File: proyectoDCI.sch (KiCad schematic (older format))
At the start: 0 parts

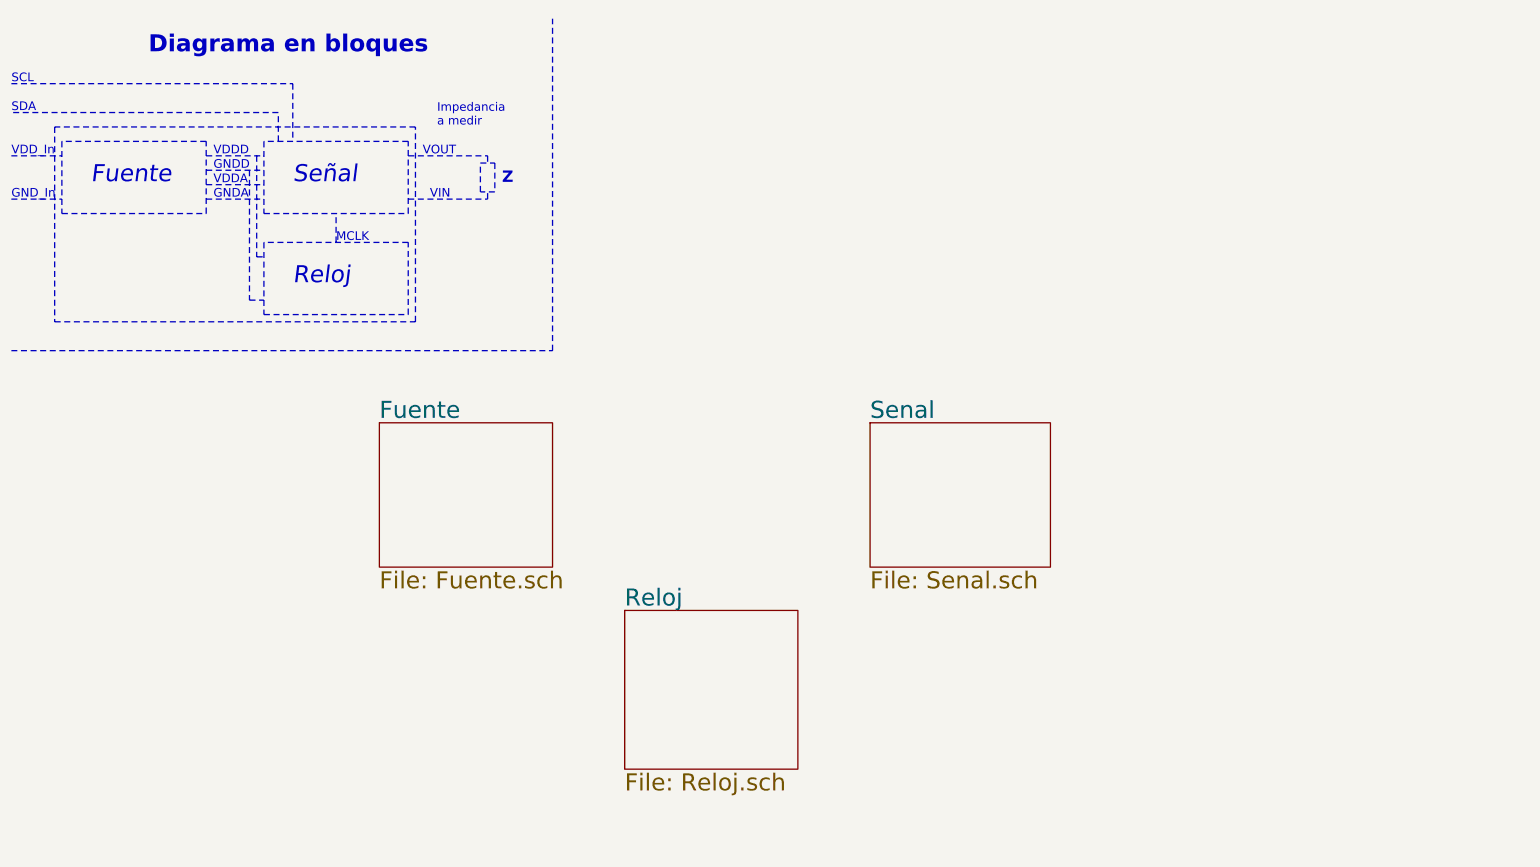
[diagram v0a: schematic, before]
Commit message: Se termino el diagrama general y se agrego texto explicativo.
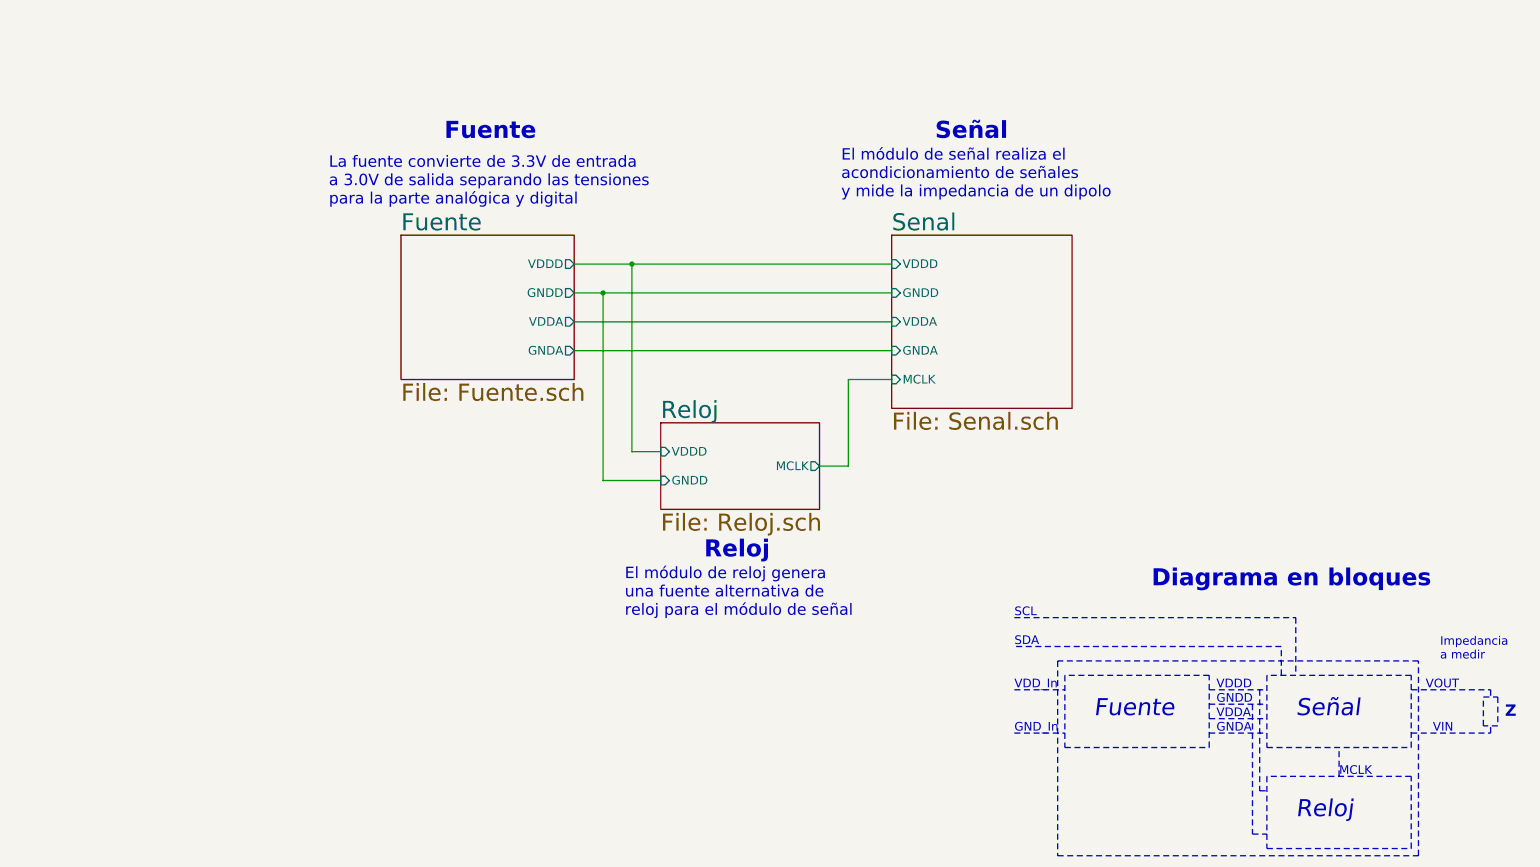
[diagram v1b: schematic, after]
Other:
- note added: "El módulo de reloj genera\nuna fuente alternativa de \nreloj para el módulo de señal"
- note added: "El módulo de señal realiza el \nacondicionamiento de señales \ny mide la impedancia de un dipolo"
- note added: "La fuente convierte de 3.3V de entrada \na 3.0V de salida separando las tensiones\npara la parte analógica y digital"
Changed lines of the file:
@@
 LIBS:contrib
 LIBS:valves
+LIBS:proyectoDCI-cache
 EELAYER 25 0
 EELAYER END
 $Descr A4 11693 8268
 encoding utf-8
-Sheet 1 3
+Sheet 1 4
 Title "Medidor de impedancia (PMOD)"
 Date "2016-11-17"
@@
 Comment4 ""
 $EndDescr
-Text Notes 1500 850  0    118  ~ 24
+Text Notes 8450 4550 0    118  ~ 24
 Diagrama en bloques
-Text Notes 1100 1750 0    118  Italic 0
+Text Notes 8050 5450 0    118  Italic 0
 Fuente
-Text Notes 2500 1750 0    118  Italic 0
+Text Notes 9450 5450 0    118  Italic 0
 Señal
-Text Notes 2500 2450 0    118  Italic 0
+Text Notes 9450 6150 0    118  Italic 0
 Reloj
 Wire Notes Line
-	900  1450 900  1950
+	7850 5150 7850 5650
 Wire Notes Line
-	900  1950 1900 1950
+	7850 5650 8850 5650
 Wire Notes Line
-	1900 1950 1900 1450
+	8850 5650 8850 5150
 Wire Notes Line
-	1900 1450 900  1450
+	8850 5150 7850 5150
 Wire Notes Line
-	2300 1450 2300 1950
+	9250 5150 9250 5650
 Wire Notes Line
-	2300 1950 3300 1950
+	9250 5650 10250 5650
 Wire Notes Line
-	3300 1950 3300 1450
+	10250 5650 10250 5150
 Wire Notes Line
-	3300 1450 2300 1450
+	10250 5150 9250 5150
 Wire Notes Line
-	2300 2150 2300 2650
+	9250 5850 9250 6350
 Wire Notes Line
-	2300 2650 3300 2650
+	9250 6350 10250 6350
 Wire Notes Line
-	3300 2650 3300 2150
+	10250 6350 10250 5850
 Wire Notes Line
-	3300 2150 2300 2150
+	10250 5850 9250 5850
 Wire Notes Line
-	550  1550 900  1550
+	7500 5250 7850 5250
 Wire Notes Line
-	550  1850 900  1850
-Text Notes 550  1550 0    60   ~ 0
+	7500 5550 7850 5550
+Text Notes 7500 5250 0    60   ~ 0
 VDD_In
-Text Notes 550  1850 0    60   ~ 0
+Text Notes 7500 5550 0    60   ~ 0
 GND_In
 Wire Notes Line
-	1900 1550 2300 1550
+	8850 5250 9250 5250
 Wire Notes Line
-	1900 1650 2300 1650
+	8850 5350 9250 5350
 Wire Notes Line
-	1900 1750 2300 1750
+	8850 5450 9250 5450
 Wire Notes Line
-	1900 1850 2300 1850
-Text Notes 1950 1550 0    60   ~ 0
+	8850 5550 9250 5550
+Text Notes 8900 5250 0    60   ~ 0
 VDDD
-Text Notes 1950 1650 0    60   ~ 0
+Text Notes 8900 5350 0    60   ~ 0
 GNDD\n
-Text Notes 1950 1750 0    60   ~ 0
+Text Notes 8900 5450 0    60   ~ 0
 VDDA
-Text Notes 1950 1850 0    60   ~ 0
+Text Notes 8900 5550 0    60   ~ 0
 GNDA
-Text Notes 3400 1550 0    60   ~ 0
+Text Notes 10350 5250 0    60   ~ 0
 VOUT
-Text Notes 3450 1850 0    60   ~ 0
+Text Notes 10400 5550 0    60   ~ 0
 VIN\n
 Wire Notes Line
-	3300 1550 3850 1550
+	10250 5250 10800 5250
 Wire Notes Line
-	3300 1850 3850 1850
+	10250 5550 10800 5550
 Wire Notes Line
-	2250 1550 2250 2250
+	9200 5250 9200 5950
 Wire Notes Line
-	2250 2250 2300 2250
+	9200 5950 9250 5950
 Wire Notes Line
-	2200 1650 2200 2550
+	9150 5350 9150 6250
 Wire Notes Line
-	2200 2550 2300 2550
-Text Notes 2800 2150 0    60   ~ 0
+	9150 6250 9250 6250
+Text Notes 9750 5850 0    60   ~ 0
 MCLK
 Wire Notes Line
-	2800 2150 2800 1950
+	9750 5850 9750 5650
 Wire Notes Line
-	850  1350 850  2700
+	7800 5050 7800 6400
 Wire Notes Line
-	850  2700 3350 2700
+	7800 6400 10300 6400
 Wire Notes Line
-	3350 2700 3350 1350
+	10300 6400 10300 5050
 Wire Notes Line
-	3350 1350 850  1350
+	10300 5050 7800 5050
 Wire Notes Line
-	3800 1600 3900 1600
+	10750 5300 10850 5300
 Wire Notes Line
-	3900 1600 3900 1800
+	10850 5300 10850 5500
 Wire Notes Line
-	3900 1800 3800 1800
+	10850 5500 10750 5500
 Wire Notes Line
-	3800 1800 3800 1600
+	10750 5500 10750 5300
 Wire Notes Line
-	3850 1550 3850 1600
+	10800 5250 10800 5300
 Wire Notes Line
-	3850 1850 3850 1800
-Text Notes 3950 1750 0    79   ~ 16
+	10800 5550 10800 5500
+Text Notes 10900 5450 0    79   ~ 16
 Z
-Text Notes 3500 1350 0    59   ~ 0
+Text Notes 10450 5050 0    59   ~ 0
 Impedancia\na medir
 Wire Notes Line
-	2400 1450 2400 1250
+	9350 5150 9350 4950
 Wire Notes Line
-	2400 1250 550  1250
+	9350 4950 7500 4950
 Wire Notes Line
-	550  1050 2500 1050
+	7500 4750 9450 4750
 Wire Notes Line
-	2500 1050 2500 1450
-Text Notes 550  1050 0    60   ~ 0
+	9450 4750 9450 5150
+Text Notes 7500 4750 0    60   ~ 0
 SCL
-Text Notes 550  1250 0    60   ~ 0
+Text Notes 7500 4950 0    60   ~ 0
 SDA
-Wire Notes Line
-	550  2900 4300 2900
-Wire Notes Line
-	4300 2900 4300 600
 $Sheet
-S 3100 3400 1200 1000
+S 6650 2100 1250 1200
+U 582DA8FF
+F0 "Senal" 118
+F1 "Senal.sch" 118
+F2 "VDDD" I L 6650 2300 60
+F3 "GNDD" I L 6650 2500 60
+F4 "VDDA" I L 6650 2700 60
+F5 "GNDA" I L 6650 2900 60
+F6 "MCLK" I L 6650 3100 60
+$EndSheet
+$Sheet
+S 5050 3400 1100 600
+U 582DA934
+F0 "Reloj" 118
+F1 "Reloj.sch" 118
+F2 "VDDD" I L 5050 3600 60
+F3 "GNDD" I L 5050 3800 60
+F4 "MCLK" O R 6150 3700 60
+$EndSheet
+Wire Wire Line
+	4450 2300 6650 2300
+Wire Wire Line
+	4450 2500 6650 2500
+Wire Wire Line
+	4450 2700 6650 2700
+Wire Wire Line
+	4450 2900 6650 2900
+Wire Wire Line
+	5050 3800 4650 3800
+Wire Wire Line
+	4650 3800 4650 2500
+Connection ~ 4650 2500
+Wire Wire Line
+	5050 3600 4850 3600
+Wire Wire Line
+	4850 3600 4850 2300
+Connection ~ 4850 2300
+Wire Wire Line
+	6150 3700 6350 3700
+Wire Wire Line
+	6350 3700 6350 3100
+Wire Wire Line
+	6350 3100 6650 3100
+$Sheet
+S 3250 2100 1200 1000
 U 582DA8A0
 F0 "Fuente" 118
 F1 "Fuente.sch" 118
+F2 "VDDD" O R 4450 2300 60
+F3 "GNDD" O R 4450 2500 60
+F4 "VDDA" O R 4450 2700 60
+F5 "GNDA" O R 4450 2900 60
 $EndSheet
-$Sheet
-S 6500 3400 1250 1000
-U 582DA8FF
-F0 "Senal" 118
-F1 "Senal.sch" 118
-$EndSheet
-$Sheet
-S 4800 4700 1200 1100
-U 582DA934
-F0 "Reloj" 118
-F1 "Reloj.sch" 118
-$EndSheet
+Text Notes 3550 1450 0    118  ~ 24
+Fuente
+Text Notes 2750 1900 0    79   ~ 0
+La fuente convierte de 3.3V de entrada \na 3.0V de salida separando las tensiones\npara la parte analógica y digital
+Text Notes 6950 1450 0    118  ~ 24
+Señal
+Text Notes 6300 1850 0    79   ~ 0
+El módulo de señal realiza el \nacondicionamiento de señales \ny mide la impedancia de un dipolo
+Text Notes 5350 4350 0    118  ~ 24
+Reloj
+Text Notes 4800 4750 0    79   ~ 0
+El módulo de reloj genera\nuna fuente alternativa de \nreloj para el módulo de señal
 $EndSCHEMATC

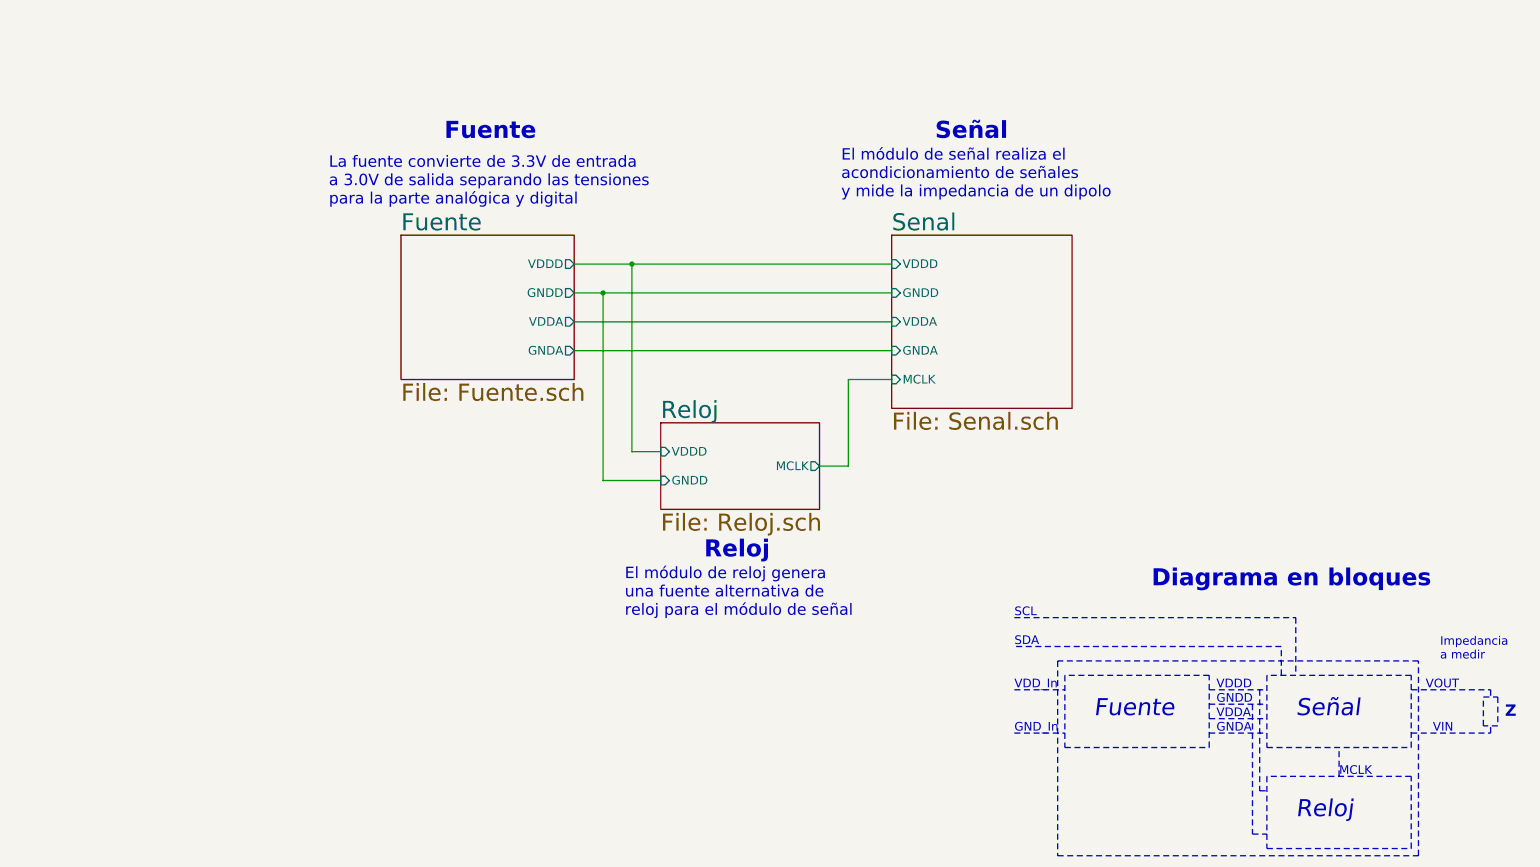
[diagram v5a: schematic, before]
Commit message: Reformulado el esquematico para contener el diseño en dos hojas
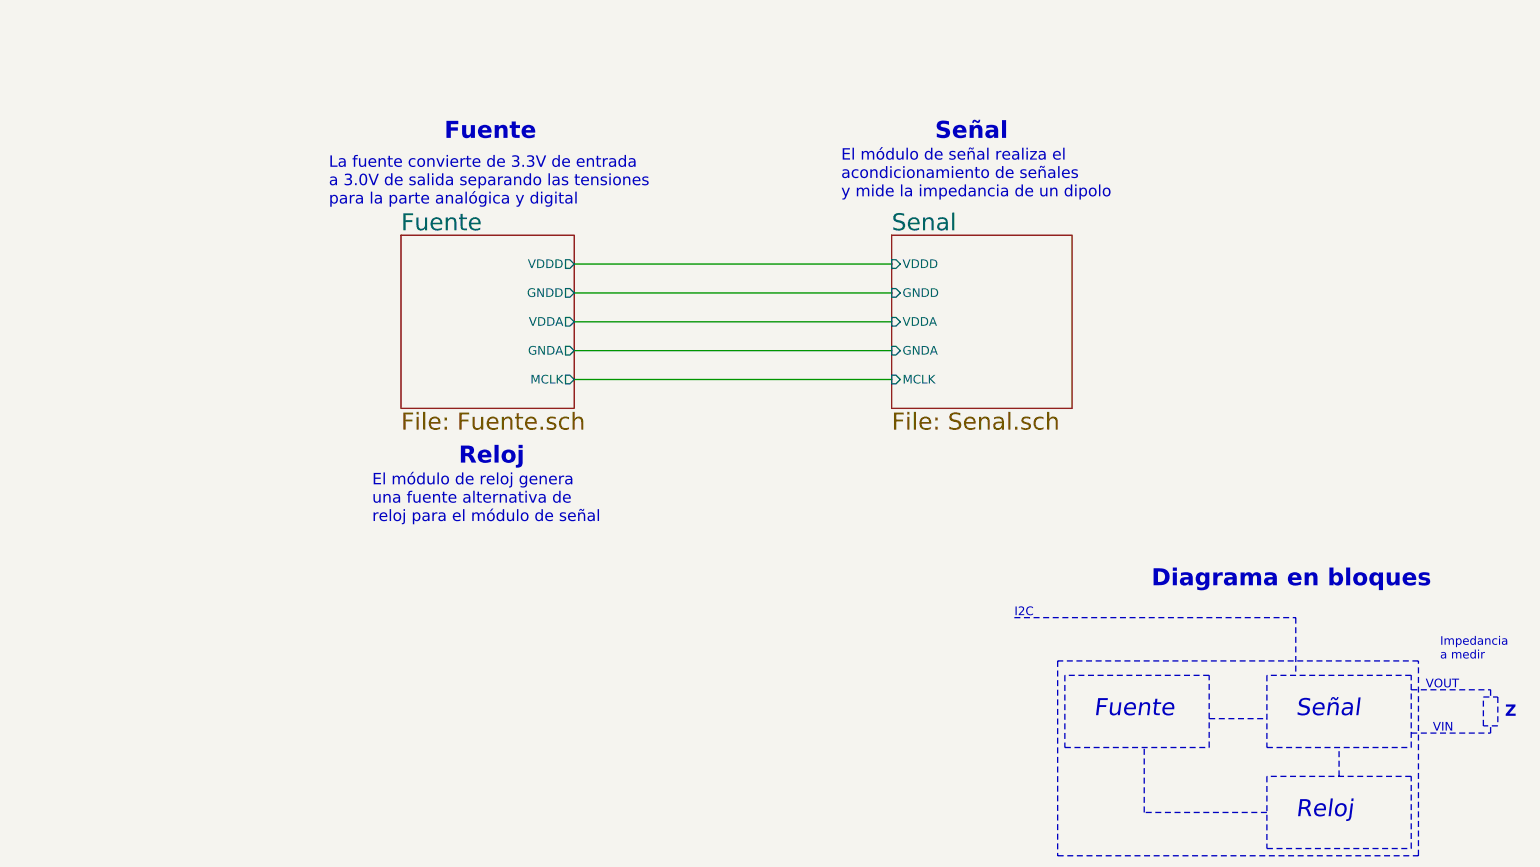
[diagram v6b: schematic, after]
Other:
- note added: "I2C"
- note removed: "GNDA"
- note removed: "GNDD\n"
- note removed: "GND_In"
- note removed: "MCLK"
- note removed: "SCL"
- note removed: "SDA"
- note removed: "VDDA"
- note removed: "VDDD"
- note removed: "VDD_In"
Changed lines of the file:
@@
 $Descr A4 11693 8268
 encoding utf-8
-Sheet 1 4
+Sheet 1 3
 Title "Medidor de impedancia (PMOD)"
 Date "2016-11-17"
@@
 	10250 5850 9250 5850
 Wire Notes Line
-	7500 5250 7850 5250
-Wire Notes Line
-	7500 5550 7850 5550
-Text Notes 7500 5550 0    60   ~ 0
-GND_In
-Wire Notes Line
-	8850 5250 9250 5250
-Wire Notes Line
-	8850 5350 9250 5350
-Wire Notes Line
 	8850 5450 9250 5450
-Wire Notes Line
-	8850 5550 9250 5550
-Text Notes 8900 5350 0    60   ~ 0
-GNDD\n
-Text Notes 8900 5450 0    60   ~ 0
-VDDA
-Text Notes 8900 5550 0    60   ~ 0
-GNDA
 Text Notes 10350 5250 0    60   ~ 0
 VOUT
@@
 Wire Notes Line
 	10250 5550 10800 5550
-Wire Notes Line
-	9200 5250 9200 5950
-Wire Notes Line
-	9200 5950 9250 5950
-Wire Notes Line
-	9150 5350 9150 6250
-Wire Notes Line
-	9150 6250 9250 6250
-Text Notes 9750 5850 0    60   ~ 0
-MCLK
 Wire Notes Line
 	9750 5850 9750 5650
@@
 Impedancia\na medir
 Wire Notes Line
-	9350 5150 9350 4950
-Wire Notes Line
-	9350 4950 7500 4950
-Wire Notes Line
 	7500 4750 9450 4750
 Wire Notes Line
 	9450 4750 9450 5150
 Text Notes 7500 4750 0    60   ~ 0
-SCL
-Text Notes 7500 4950 0    60   ~ 0
-SDA
+I2C
 $Sheet
 S 6650 2100 1250 1200
@@
 F6 "MCLK" I L 6650 3100 60
 $EndSheet
-$Sheet
-S 5050 3400 1100 600
-U 582DA934
-F0 "Reloj" 118
-F1 "Reloj.sch" 118
-F2 "VDDD" I L 5050 3600 60
-F3 "GNDD" I L 5050 3800 60
-F4 "MCLK" O R 6150 3700 60
-$EndSheet
 Wire Wire Line
 	4450 2300 6650 2300
@@
 Wire Wire Line
 	4450 2900 6650 2900
-Wire Wire Line
-	5050 3800 4650 3800
-Wire Wire Line
-	4650 3800 4650 2500
-Connection ~ 4650 2500
-Wire Wire Line
-	5050 3600 4850 3600
-Wire Wire Line
-	4850 3600 4850 2300
-Connection ~ 4850 2300
-Wire Wire Line
-	6150 3700 6350 3700
-Wire Wire Line
-	6350 3700 6350 3100
-Wire Wire Line
-	6350 3100 6650 3100
-$Sheet
-S 3250 2100 1200 1000
-U 582DA8A0
-F0 "Fuente" 118
-F1 "Fuente.sch" 118
-F2 "VDDD" O R 4450 2300 60
-F3 "GNDD" O R 4450 2500 60
-F4 "VDDA" O R 4450 2700 60
-F5 "GNDA" O R 4450 2900 60
-$EndSheet
 Text Notes 3550 1450 0    118  ~ 24
 Fuente
@@
 Text Notes 6300 1850 0    79   ~ 0
 El módulo de señal realiza el \nacondicionamiento de señales \ny mide la impedancia de un dipolo
-Text Notes 5350 4350 0    118  ~ 24
+Text Notes 3650 3700 0    118  ~ 24
 Reloj
-Text Notes 4800 4750 0    79   ~ 0
+Text Notes 3050 4100 0    79   ~ 0
 El módulo de reloj genera\nuna fuente alternativa de \nreloj para el módulo de señal
-Text Notes 8900 5250 0    60   ~ 0
-VDDD
-Text Notes 7500 5250 0    60   ~ 0
-VDD_In
+Wire Notes Line
+	9250 6100 8400 6100
+Wire Notes Line
+	8400 6100 8400 5650
+$Sheet
+S 3250 2100 1200 1200
+U 582DA8A0
+F0 "Fuente" 118
+F1 "Fuente.sch" 118
+F2 "VDDD" O R 4450 2300 60
+F3 "GNDD" O R 4450 2500 60
+F4 "VDDA" O R 4450 2700 60
+F5 "GNDA" O R 4450 2900 60
+F6 "MCLK" O R 4450 3100 60
+$EndSheet
+Wire Wire Line
+	4450 3100 6650 3100
 $EndSCHEMATC
